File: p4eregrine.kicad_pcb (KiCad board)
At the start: 6 copper layers, 39.5 x 39.5 mm, 359 parts, among them J5 Conn_Coaxial, Q10 NMOS, Q11 NMOS, Q12 NMOS, Q13 NMOS, Q14 NMOS, Q15 NMOS, Q16 NMOS, Q17 NMOS, Q18 NMOS, Q19 NMOS, Q20 NMOS, Q21 NMOS, Q22 NMOS, Q23 NMOS, Q24 NMOS, Q25 NMOS, Q26 NMOS, Q27 NMOS, Q28 NMOS, Q5 NMOS, Q6 NMOS, Q7 NMOS, Q8 NMOS, Q9 NMOS, U1 ESP32-P4NRW32X, U10 FPC-1.0FX-15PWCR-H20, U11 VL53L1CXV0FY1, U12 LIS2MDL, U13 LSM6DS3, U14 PMW3901MB-TXQT_C43496881, U15 TPD2EUSB30A, U16 DRV8328ARUYR, U17 TPS62933, U19 DRV8328ARUYR, U2 LPS22HB, U20 STM32G071GBU6, U22 DRV8328ARUYR, U23 STM32G071GBU6, U25 DRV8328ARUYR, U26 STM32G071GBU6, U3 W25Q128JVP, U30 STM32G071GBU6, U4 ESP32-C5HF4, U5 LFD182G45DCHD277, U6 TLV62569DBV, U8 INA190A2IDCKR, U9 TPS2121RUXR, Y1 Crystal_GND24, Y2 Crystal_GND24

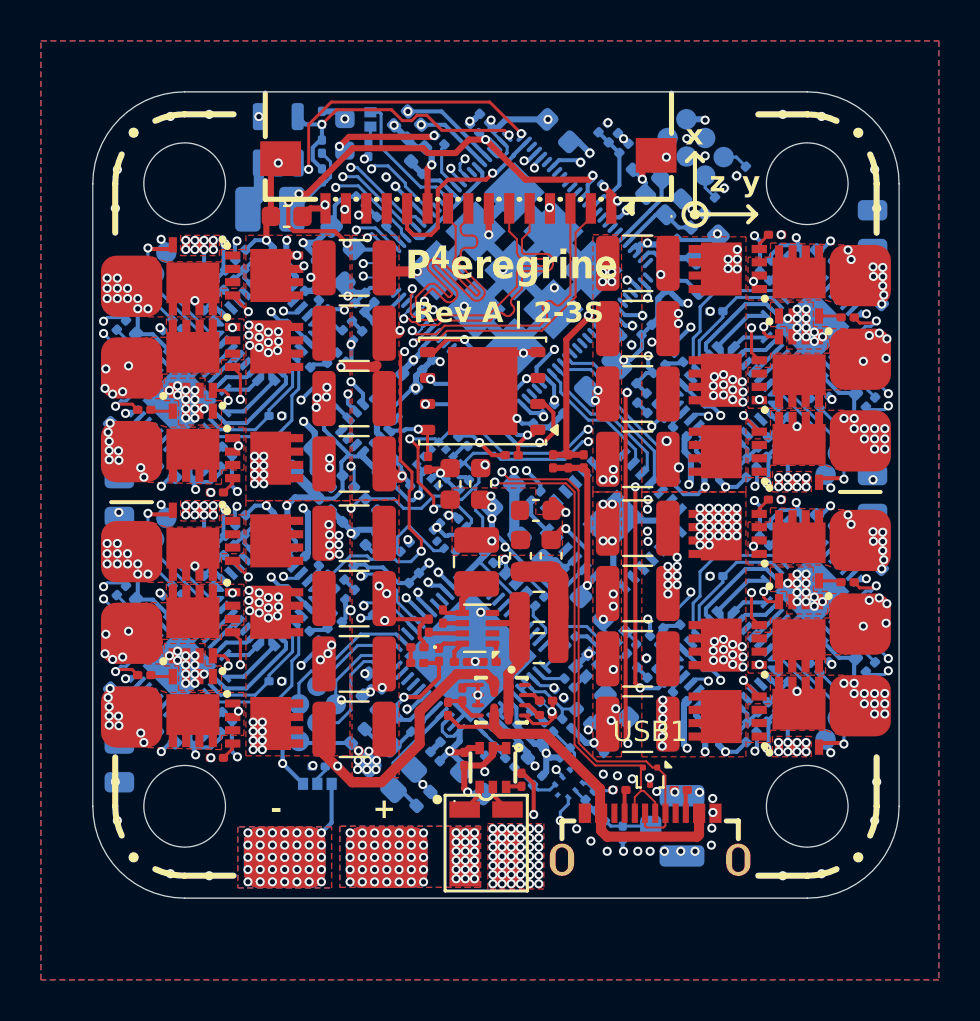
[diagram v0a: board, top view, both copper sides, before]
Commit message: Make GND probe pads square
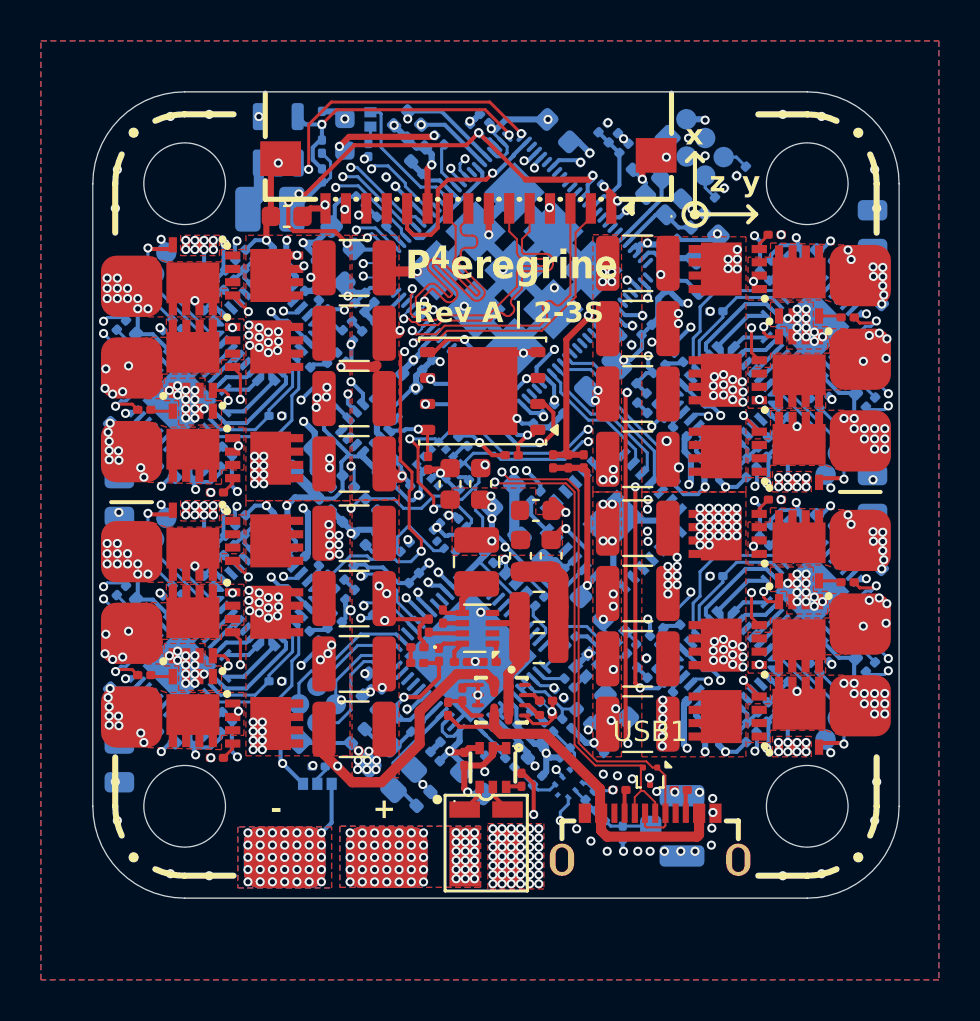
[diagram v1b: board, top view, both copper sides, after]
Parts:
- TP38, TP48: footprint easyeda2kicad:TestPoint_Pad_D1.0mm_No_Courtyard -> easyeda2kicad:TestPoint_Pad_L1.0mm
- turned TP38 to 135 degrees
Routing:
- net VDDO_4: track 30.5 -> 31.3 mm
- net VDD_HP: track 42.7 -> 43.3 mm
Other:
- board text added: "ck"
- board text added: "di"
- board text added: "do"
- board text added: "ms"
- board text added: "rx"
- board text added: "sda"

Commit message: Add VDD_HP testpoint
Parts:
- added TP51: TestPoint, easyeda2kicad:TestPoint_Pad_D1.0mm_No_Courtyard, B.Cu at (137.0, 72.2)
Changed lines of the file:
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@@
 		)
+	)
+	(footprint "easyeda2kicad:TestPoint_Pad_D1.0mm_No_Courtyard"
+		(layer "B.Cu")
+		(at 137 72.2 180)
+		(descr "SMD pad as test Point, diameter 1.0mm")
+		(tags "test point SMD pad")
+		(property "Reference" "TP51"
+			(at 0 1.448 0)
+			(layer "B.SilkS")
+			(hide yes)
+			(effects
+				(font
+					(size 1 1)
+					(thickness 0.15)
+				)
+				(justify mirror)
+			)
+		)
+		(property "Value" "TestPoint"
+			(at 0 -1.55 0)
+			(layer "B.Fab")
+			(effects
+				(font
+					(size 1 1)
+					(thickness 0.15)
+				)
+				(justify mirror)
+			)
+		)
+		(property "Datasheet" ""
+			(at 0 0 0)
+			(unlocked yes)
+			(layer "B.Fab")
+			(hide yes)
+			(effects
+				(font
+					(size 1.27 1.27)
+					(thickness 0.15)
+				)
+				(justify mirror)
+			)
+		)
+		(property "Description" "test point"
+			(at 0 0 0)
+			(unlocked yes)
+			(layer "B.Fab")
+			(hide yes)
+			(effects
+				(font
+					(size 1.27 1.27)
+					(thickness 0.15)
+				)
+				(justify mirror)
+			)
+		)
+		(property "KLC_S3.3" ""
+			(at 0 0 0)
+			(unlocked yes)
+			(layer "B.Fab")
+			(hide yes)
+			(effects
+				(font
+					(size 1 1)
+					(thickness 0.15)
+				)
+				(justify mirror)
+			)
+		)
+		(property "KLC_S4.1" ""
+			(at 0 0 0)
+			(unlocked yes)
+			(layer "B.Fab")
+			(hide yes)
+			(effects
+				(font
+					(size 1 1)
+					(thickness 0.15)
+				)
+				(justify mirror)
+			)
+		)
+		(property "KLC_S5.1" ""
+			(at 0 0 0)
+			(unlocked yes)
+			(layer "B.Fab")
+			(hide yes)
+			(effects
+				(font
+					(size 1 1)
+					(thickness 0.15)
+				)
+				(justify mirror)
+			)
+		)
+		(property ki_fp_filters "Pin* Test*")
+		(sheetname "/Power/")
+		(sheetfile "power.kicad_sch")
+		(units
+			(unit
+				(name "A")
+				(pins "1")
+			)
+		)
+		(duplicate_pad_numbers_are_jumpers no)
+		(fp_text user "${REFERENCE}"
+			(at 0 1.45 0)
+			(layer "B.Fab")
+			(effects
+				(font
+					(size 1 1)
+					(thickness 0.15)
+				)
+				(justify mirror)
+			)
+		)
+		(pad "1" smd circle
+			(at 0 0 180)
+			(size 1 1)
+			(layers "B.Cu" "B.Mask")
+			(net "VDD_HP")
+			(pinfunction "1_1")
+			(pintype "passive")
+		)
+		(embedded_fonts no)
 	)
 	(footprint "Capacitor_SMD:C_0201_0603Metric"
